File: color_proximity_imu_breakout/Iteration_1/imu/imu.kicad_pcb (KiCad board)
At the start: 2 copper layers, 15 x 16.5 mm, 15 parts, among them IC2 ISL29125IROZ-T7, J4 Conn_01x05

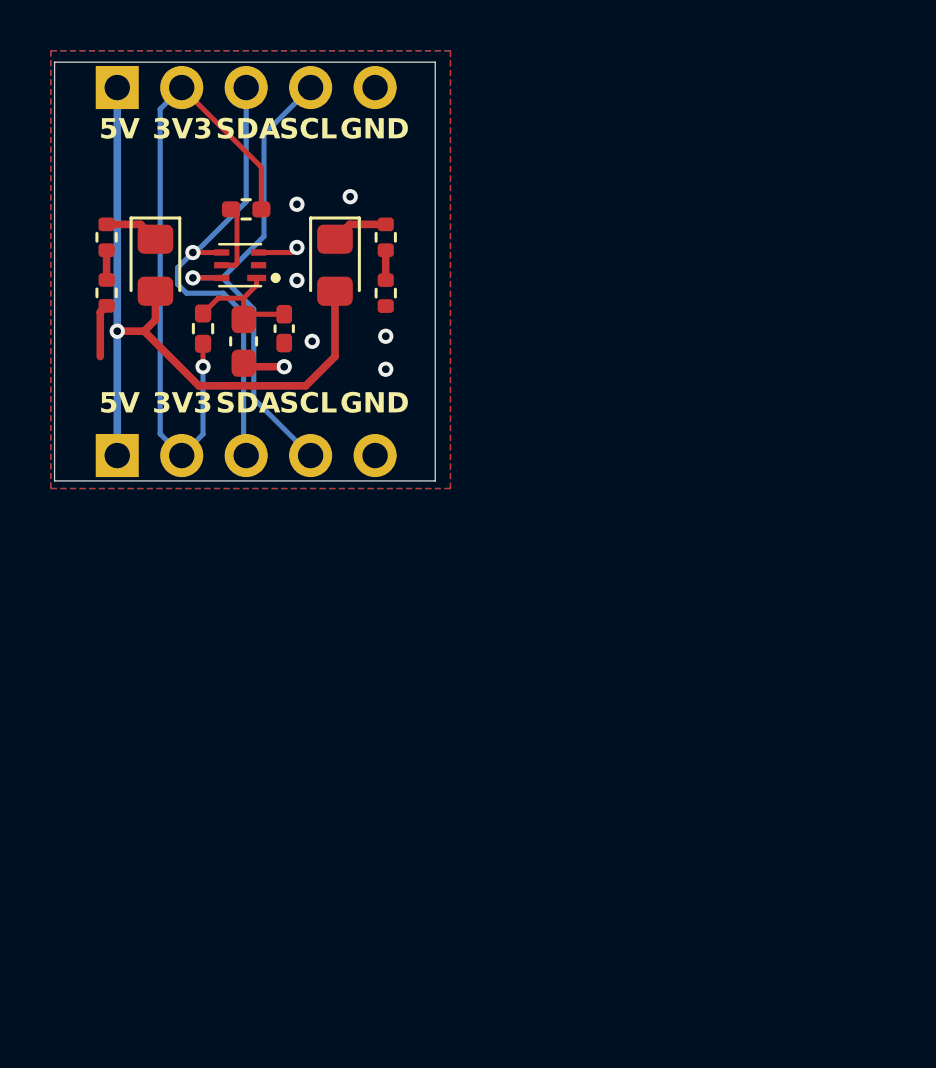
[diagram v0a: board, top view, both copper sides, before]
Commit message: Iteration 2 of color, distance, and imu sensor boards
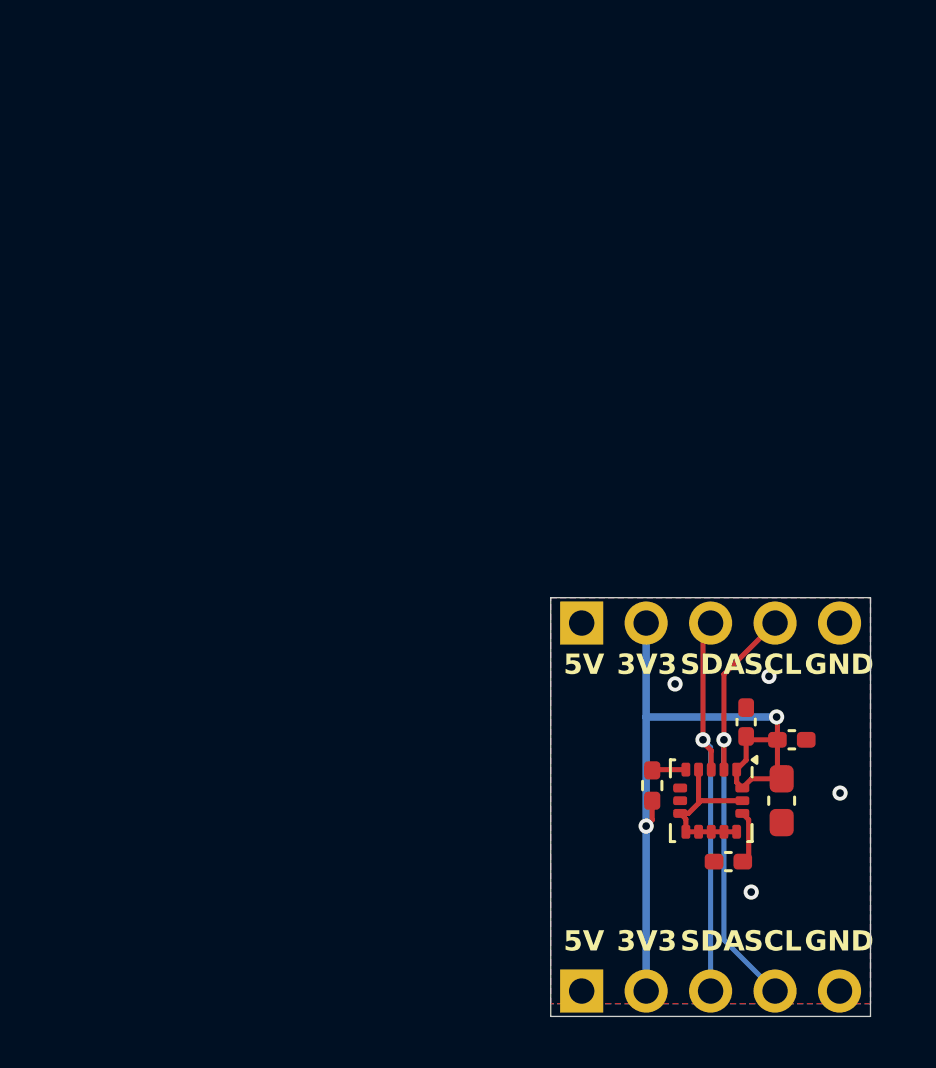
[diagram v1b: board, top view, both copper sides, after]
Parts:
- removed C4: 1u, Capacitor_SMD:C_0603_1608Metric_Pad1.08x0.95mm_HandSolder
- removed C5: 0.1u, Capacitor_SMD:C_0402_1005Metric_Pad0.74x0.62mm_HandSolder
- removed D1, D2: WHITE, LED_SMD:LED_0805_2012Metric_Pad1.15x1.40mm_HandSolder
- removed the G*** at (104.5, 108.4)
- removed the G*** at (105.2, 113.5)
- removed IC2: ISL29125IROZ-T7, ISL29125:ISL29125IROZT7
- removed the J4 at (103.1, 105.1)
- removed the J4 at (103.1, 119.6)
- removed R15: 100, Resistor_SMD:R_0402_1005Metric_Pad0.72x0.64mm_HandSolder
- removed R16: 4.7k, Resistor_SMD:R_0402_1005Metric_Pad0.72x0.64mm_HandSolder
- removed R17, R18, R30, R32: 120, Resistor_SMD:R_0402_1005Metric
- added C10: 0.1u, Capacitor_SMD:C_0402_1005Metric_Pad0.74x0.62mm_HandSolder, F.Cu at (127.2, 135.6)
- added C7: 0.1u, Capacitor_SMD:C_0402_1005Metric_Pad0.74x0.62mm_HandSolder, F.Cu at (127.9, 130.1)
- added C8: 2.2u, Capacitor_SMD:C_0603_1608Metric_Pad1.08x0.95mm_HandSolder, F.Cu at (129.3, 133.2)
- added C9: 10n, Capacitor_SMD:C_0402_1005Metric_Pad0.74x0.62mm_HandSolder, F.Cu at (129.7, 130.8)
- added G***: LOGO, LOGO, B.Cu at (122.8, 129.5)
- added G***: LOGO, LOGO, B.Cu at (124.4, 134.3)
- added J4: Conn_01x05, Connector_PinHeader_2.54mm:PinHeader_1x05_P2.54mm_Vertical, F.Cu at (121.4, 140.7)
- added J4: Conn_01x05, Connector_PinHeader_2.54mm:PinHeader_1x05_P2.54mm_Vertical, F.Cu at (121.4, 126.2)
- added R19: 4.7k, Resistor_SMD:R_0402_1005Metric_Pad0.72x0.64mm_HandSolder, F.Cu at (124.2, 132.6)
- added U6: ICM-20602, Package_LGA:LGA-16_3x3mm_P0.5mm_LayoutBorder3x5y, F.Cu at (126.5, 133.2)
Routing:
- net +5V: track 28.8 -> 0.02 mm, vias 1 -> 0
- net Net-(IC2-VDD): track 5.39 -> 0.00 mm
- net +3.3V: track 26.1 -> 29.0 mm, vias 1 -> 2
- net Net-(IC2-~{INT}): track 2.86 -> 0.00 mm
- net Net-(D2-K): track 2.62 -> 0.00 mm
- net /sda: track 18.9 -> 16.3 mm
- net Net-(D1-K): track 2.57 -> 0.00 mm
- net /scl: track 19.7 -> 17.3 mm
- net Net-(U6-REGOUT): track 0.00 -> 2.10 mm
- net GND: track 5.36 -> 6.80 mm, vias 8 -> 4
- net Net-(U6-~{CS}): track 0.00 -> 1.34 mm
- net Net-(R17-Pad2): track 1.18 -> 0.00 mm
- net Net-(R18-Pad2): track 1.17 -> 0.00 mm
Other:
- board size 15 x 16.5 mm -> 12.6 x 16.5 mm
